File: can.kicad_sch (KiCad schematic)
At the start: 22 parts, among them SW7 CVS-03B, U19 TCAN3414DR, U20 TCAN3414DR

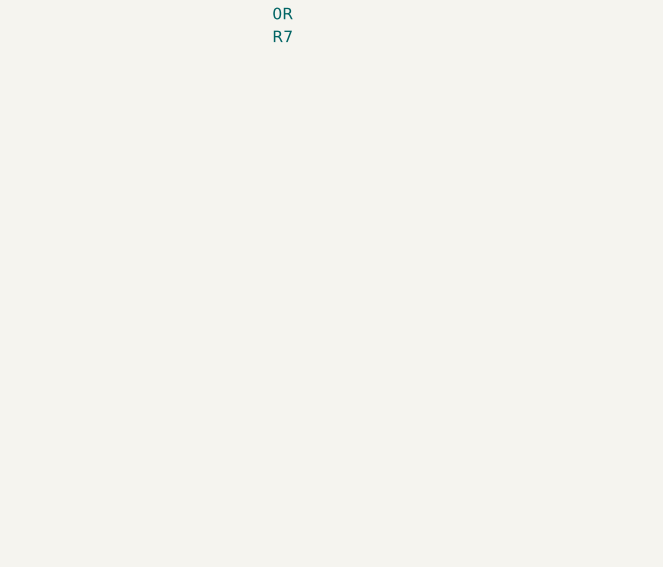
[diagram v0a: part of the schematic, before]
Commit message: [#95398] Implement BGA MCU
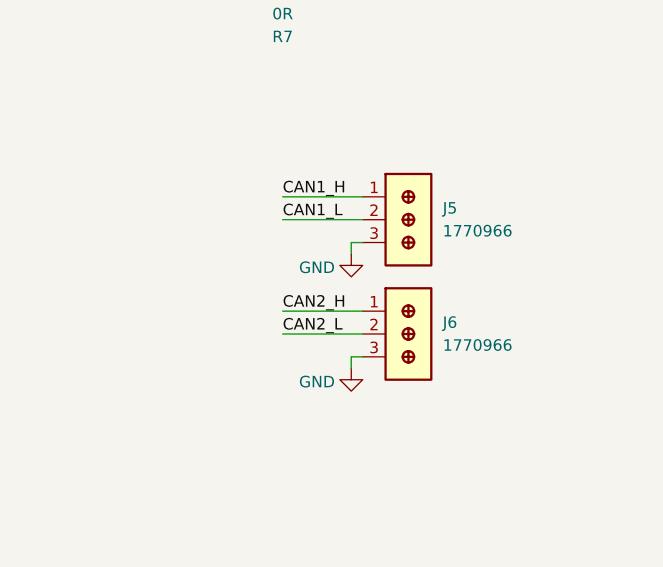
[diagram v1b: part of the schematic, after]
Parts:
- added J5, J6: Wire2Board_1x3_P2.5mm_1770966, antmicro-footprints:TerminalBlock_Wire2Board_1x3_P2.5mm_1770966, symbol antmicroTerminalBlocksConnectors:Wire2Board_1x3_P2.5mm_1770966
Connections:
- net CAN1_H: now also J5.1
- net CAN1_L: now also J5.2
- net CAN2_H: now also J6.1
- net CAN2_L: now also J6.2
- net GND: now also J5.3, J6.3

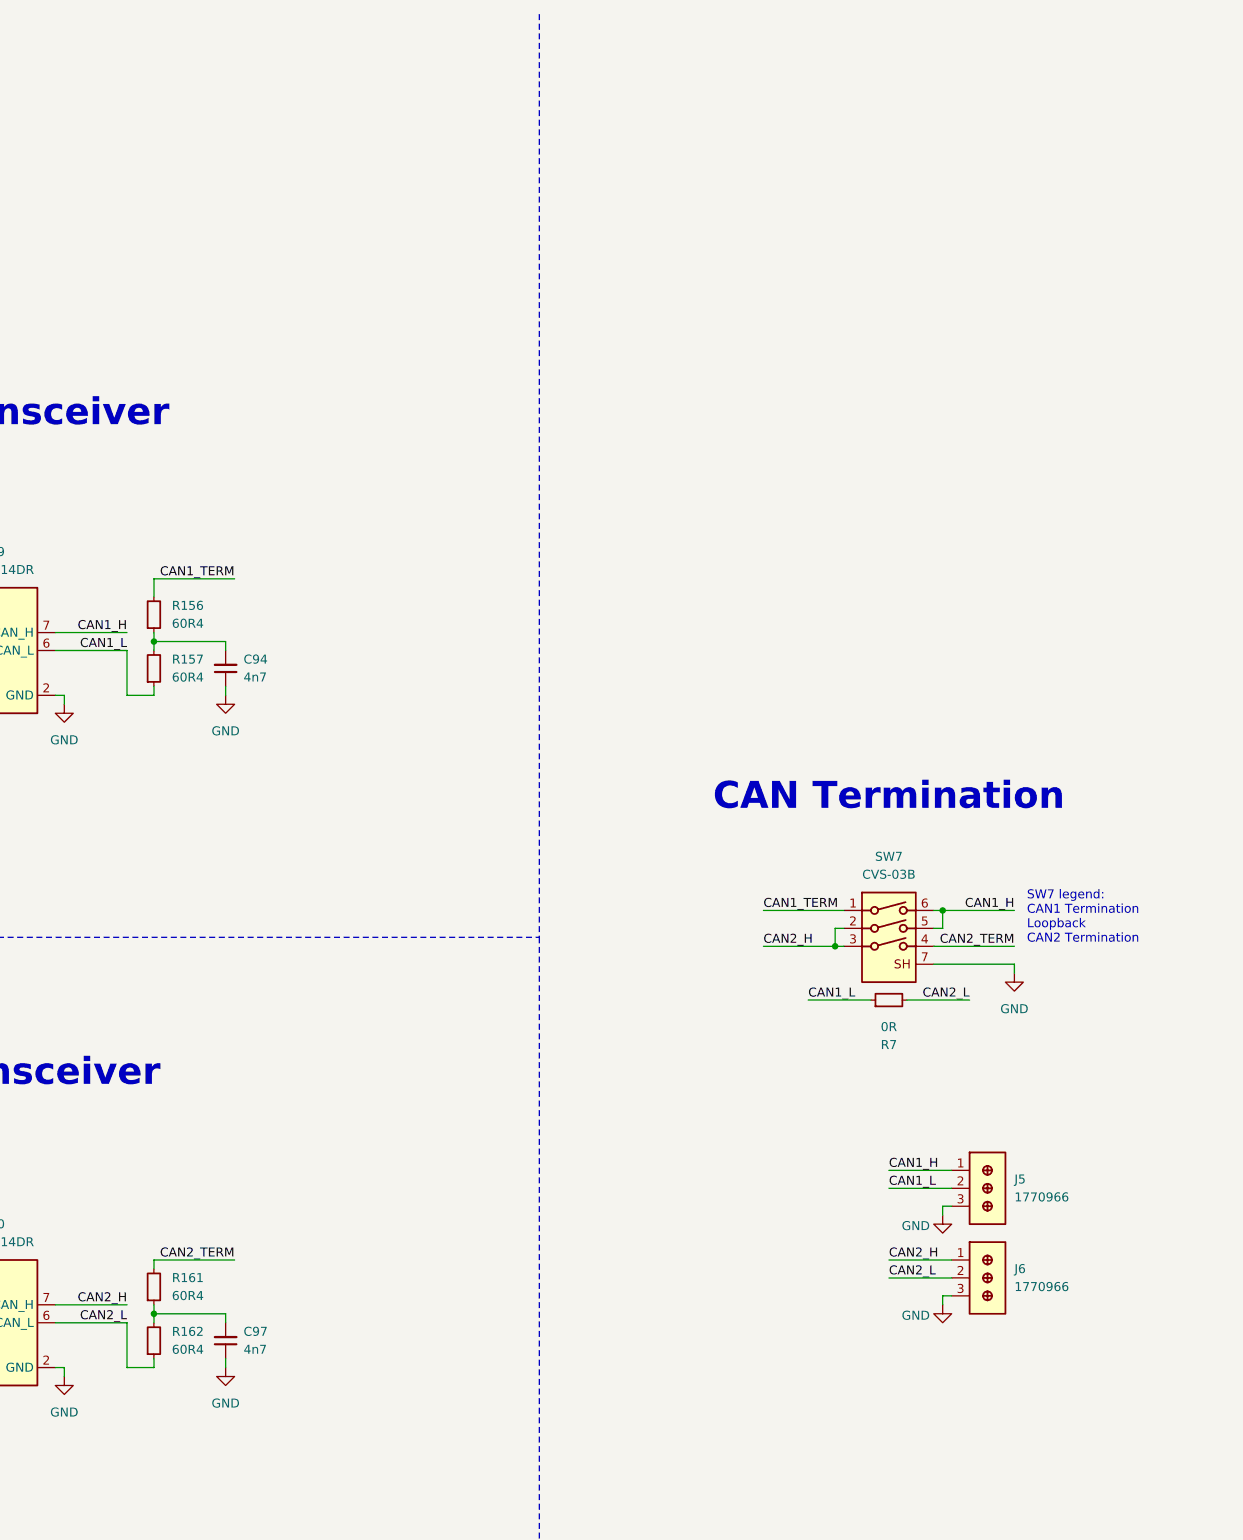
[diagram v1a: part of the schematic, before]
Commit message: [#95398] Edit CAN switching
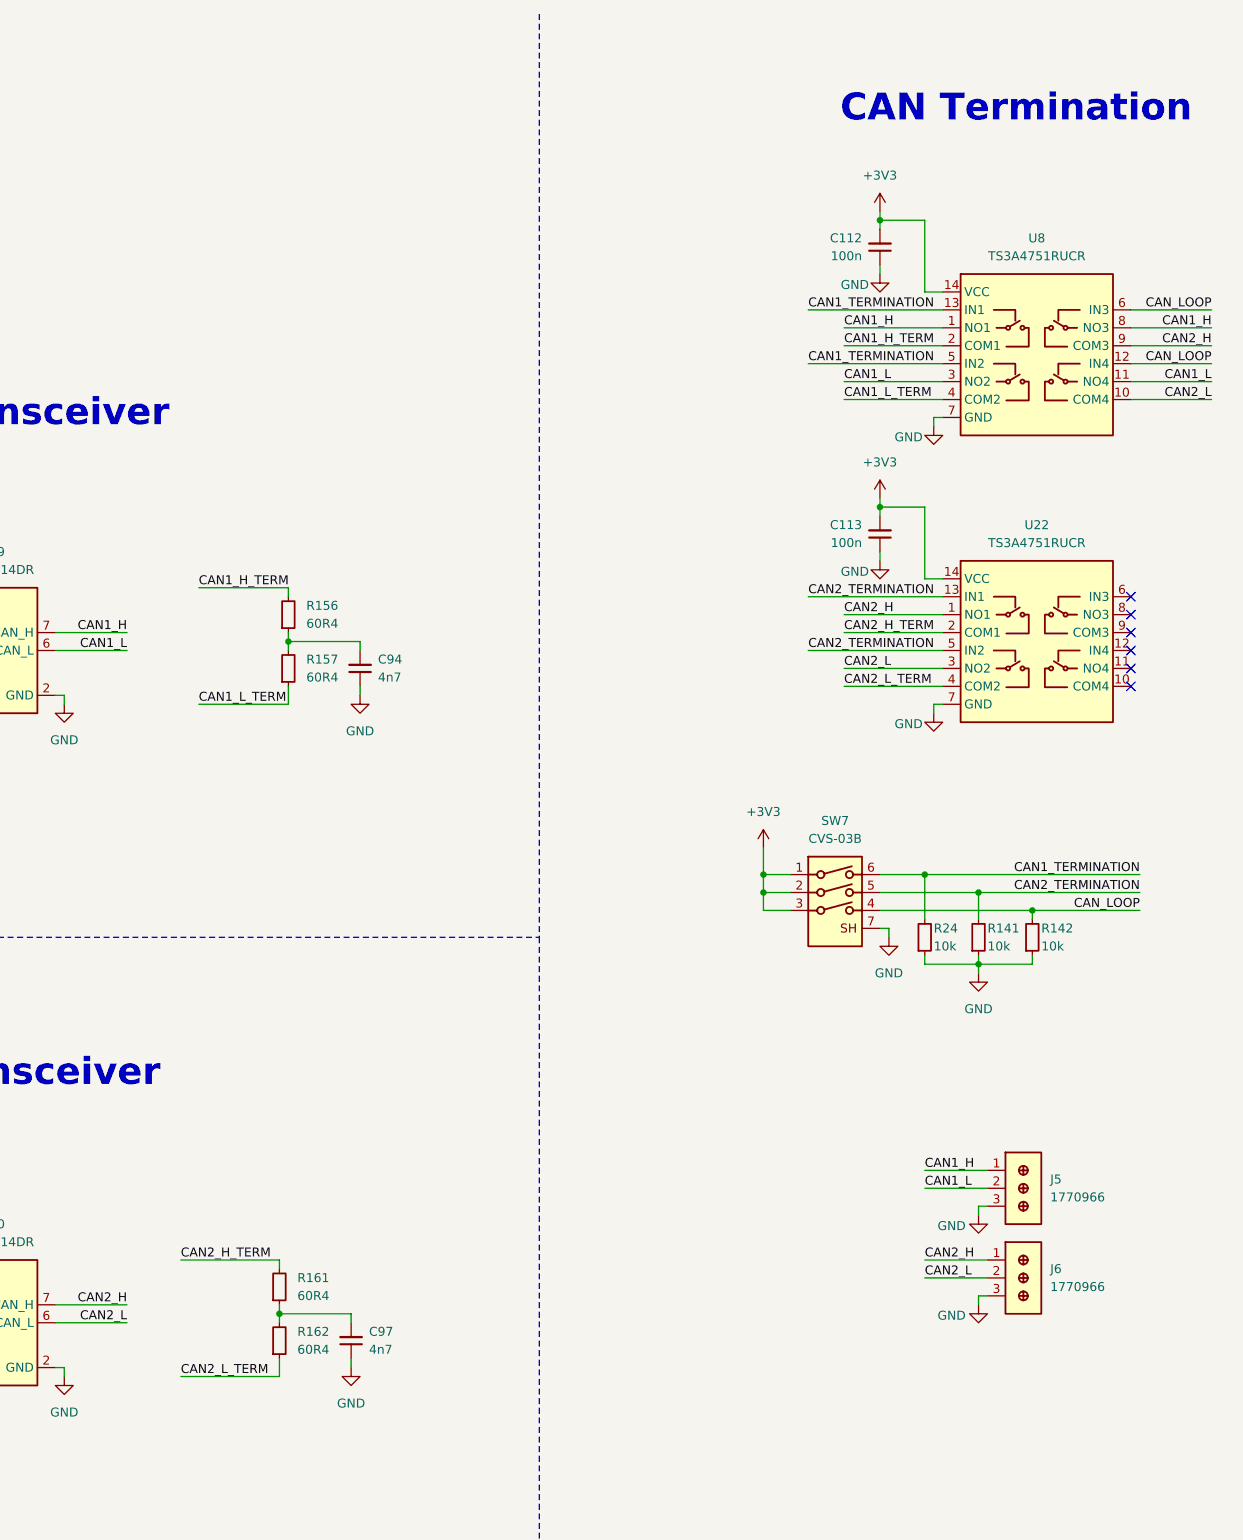
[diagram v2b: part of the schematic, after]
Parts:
- removed R7: R_0R_0402, antmicro-footprints:R_0402_1005Metric, symbol antmicroResistors0402:R_0R_0402
- added C112, C113: C_100n_0402, antmicro-footprints:C_0402_1005Metric, symbol antmicroCapacitors0402:C_100n_0402
- added R141, R142, R24: R_10k_0402, antmicro-footprints:R_0402_1005Metric, symbol antmicroResistors0402:R_10k_0402
- added U22, U8: TS3A4751_X2QFN, antmicro-footprints:Texas_X2QFN-14_2x2mm_P0.4mm, symbol antmicroInterfaceAnalogSwitchesMultiplexersDemultiplexers:TS3A4751_X2QFN
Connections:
- net +3V3: now also SW7.1, SW7.2, SW7.3, C112.2, C113.2, U22.14 (VCC), U8.14 (VCC)
- net CAN1_H: now also U8.1 (NO1), U8.8 (NO3); no longer SW7.5, SW7.6
- net CAN1_L: now also U8.11 (NO4), U8.3 (NO2); no longer R157.1
- net CAN2_H: now also U22.1 (NO1), U8.9 (COM3); no longer SW7.2, SW7.3
- net CAN2_L: now also U22.3 (NO2), U8.10 (COM4); no longer R162.1
- net GND: now also C112.1, C113.1, R141.1, R142.1, R24.1, U22.7 (GND), U8.7 (GND)
- net CAN1_TERM renamed CAN1_H_TERM
- net CAN1_H_TERM: now also U8.2 (COM1); no longer SW7.1
- net CAN2_TERM renamed CAN2_H_TERM
- net CAN2_H_TERM: now also U22.2 (COM1); no longer SW7.4
- new net CAN1_L_TERM: R157.1, U8.4 (COM2)
- new net CAN1_TERMINATION: R24.2, SW7.6, U8.13 (IN1), U8.5 (IN2)
- new net CAN2_L_TERM: R162.1, U22.4 (COM2)
- new net CAN2_TERMINATION: R141.2, SW7.5, U22.13 (IN1), U22.5 (IN2)
- new net CAN_LOOP: R142.2, SW7.4, U8.12 (IN4), U8.6 (IN3)
- no-connect marks 0 -> 6
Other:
- note removed: "SW7 legend: CAN1 Termination Loopback CAN2 Termination"
- moved on the sheet: C94, C97, J5, J6, R156, R157, R161, R162, SW7

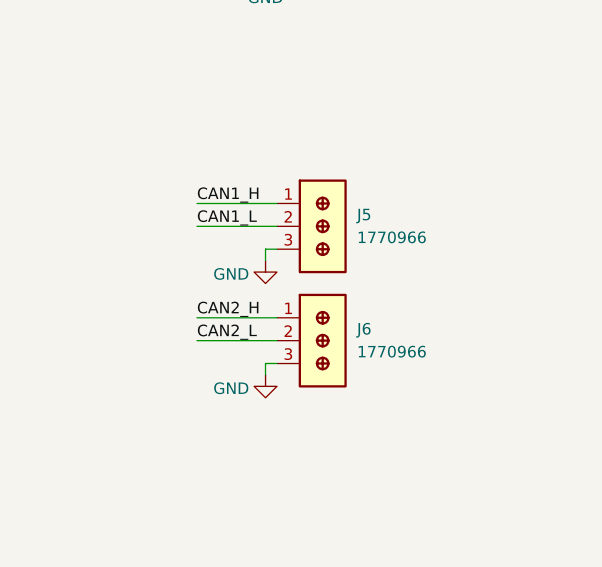
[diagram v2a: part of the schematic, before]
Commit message: [#95398] Replace CAN connectors
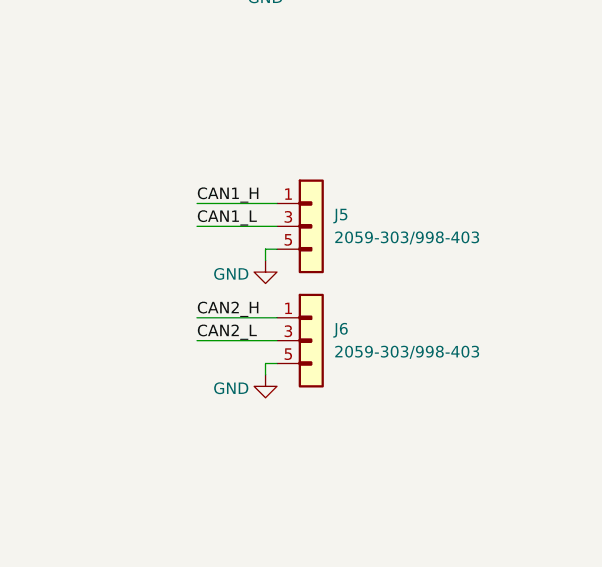
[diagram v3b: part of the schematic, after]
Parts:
- removed J5, J6: Wire2Board_1x3_P2.5mm_1770966, antmicro-footprints:TerminalBlock_Wire2Board_1x3_P2.5mm_1770966, symbol antmicroTerminalBlocksConnectors:Wire2Board_1x3_P2.5mm_1770966
- added J5, J6: Wago_2059_1x3_2059-303/998-403, antmicro-footprints:Wago_2059_1x3_2059-303-998-403, symbol antmicroWire2BoardConnectors:Wago_2059_1x3_2059-303/998-403
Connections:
- net CAN1_H: now also J5.1, J5.2
- net CAN1_L: now also J5.3, J5.4
- net CAN2_H: now also J6.1, J6.2
- net CAN2_L: now also J6.3, J6.4
- net GND: now also J5.5, J5.6, J6.5, J6.6

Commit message: [#95398] Replace WAGO connectors
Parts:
- removed J5, J6: Wago_2059_1x3_2059-303/998-403, antmicro-footprints:Wago_2059_1x3_2059-303-998-403, symbol antmicroWire2BoardConnectors:Wago_2059_1x3_2059-303/998-403
- added J5, J6: Wago_2059_1x3_2059-303/998-403, antmicro-footprints:WAGO_2059_1x3_2059-303-998-403, symbol antmicroWire2BoardConnectors:WAGO_2059_1x3_2059-303/998-403
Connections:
- net CAN1_H: now also J5.1, J5.2
- net CAN1_L: now also J5.3, J5.4
- net CAN2_H: now also J6.1, J6.2
- net CAN2_L: now also J6.3, J6.4
- net GND: now also J5.5, J5.6, J6.5, J6.6

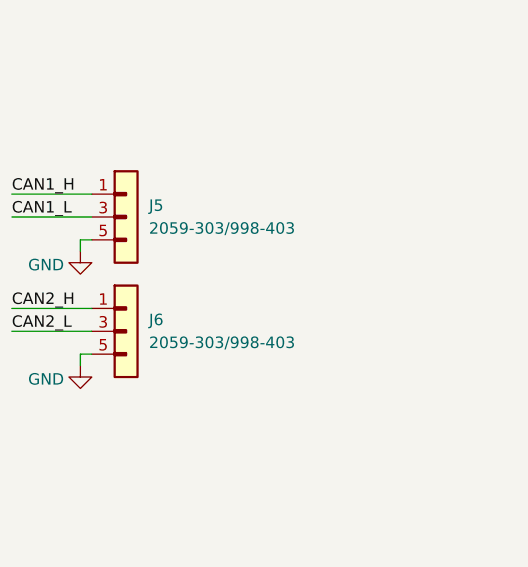
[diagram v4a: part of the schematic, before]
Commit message: [#95398] Update WAGO symbols. Add CAN 3V3 compatibility comment
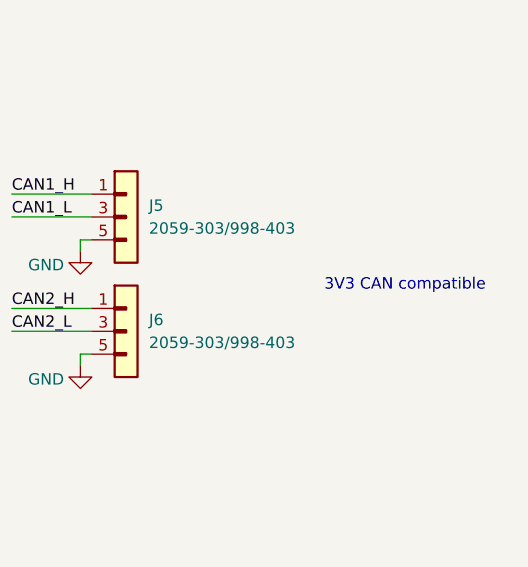
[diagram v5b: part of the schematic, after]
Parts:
- J5, J6: symbol antmicroWire2BoardConnectors:WAGO_2059_1x3_2059-303/998-403 -> Wire2BoardConnectors:WAGO_2059_1x3_2059-303-998-403
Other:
- note added: "3V3 CAN compatible"
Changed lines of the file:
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@@
 		(company "Antmicro")
 	)
+	(text "3V3 CAN compatible"
+		(exclude_from_sim no)
+		(at 333.248 186.69 0)
+		(effects
+			(font
+				(size 1.27 1.27)
+			)
+		)
+	)
 	(text "CAN2 Transceiver"
 		(exclude_from_sim no)
@@
 	)
 	(symbol
-		(lib_id "antmicroWire2BoardConnectors:WAGO_2059_1x3_2059-303/998-403")
+		(lib_id "Wire2BoardConnectors:WAGO_2059_1x3_2059-303-998-403")
 		(at 298.45 189.23 0)
 		(unit 1)
@@
 	)
 	(symbol
-		(lib_id "antmicroWire2BoardConnectors:WAGO_2059_1x3_2059-303/998-403")
+		(lib_id "Wire2BoardConnectors:WAGO_2059_1x3_2059-303-998-403")
 		(at 298.45 176.53 0)
 		(unit 1)

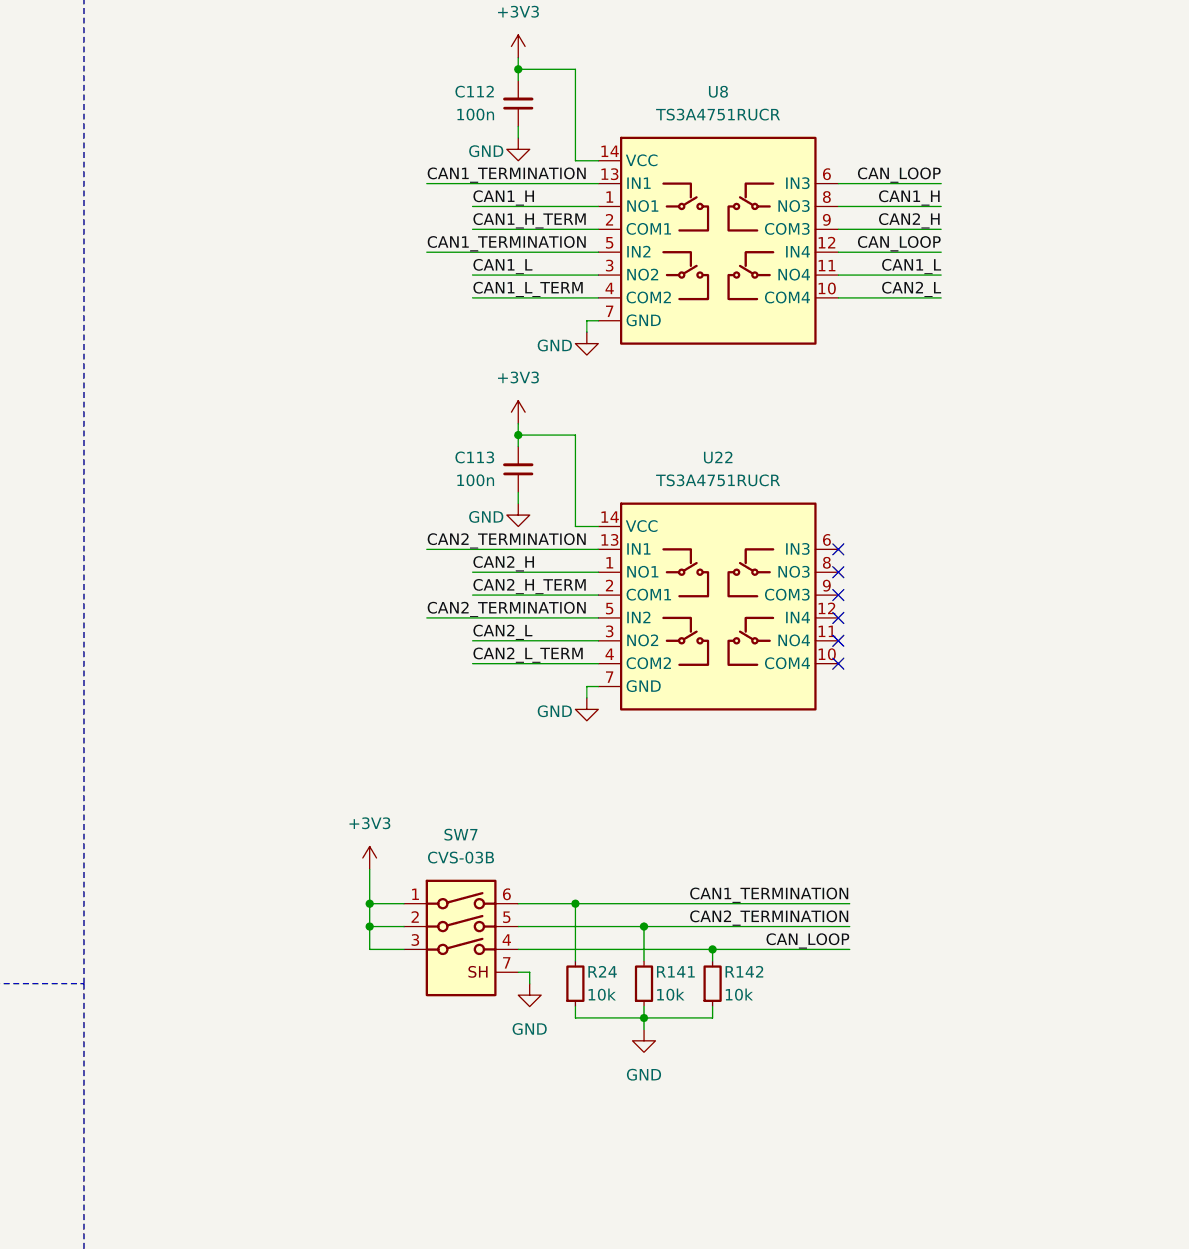
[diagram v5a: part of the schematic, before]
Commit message: [#95451] Improve placement. Add JTAG TC and ID EEPROM.
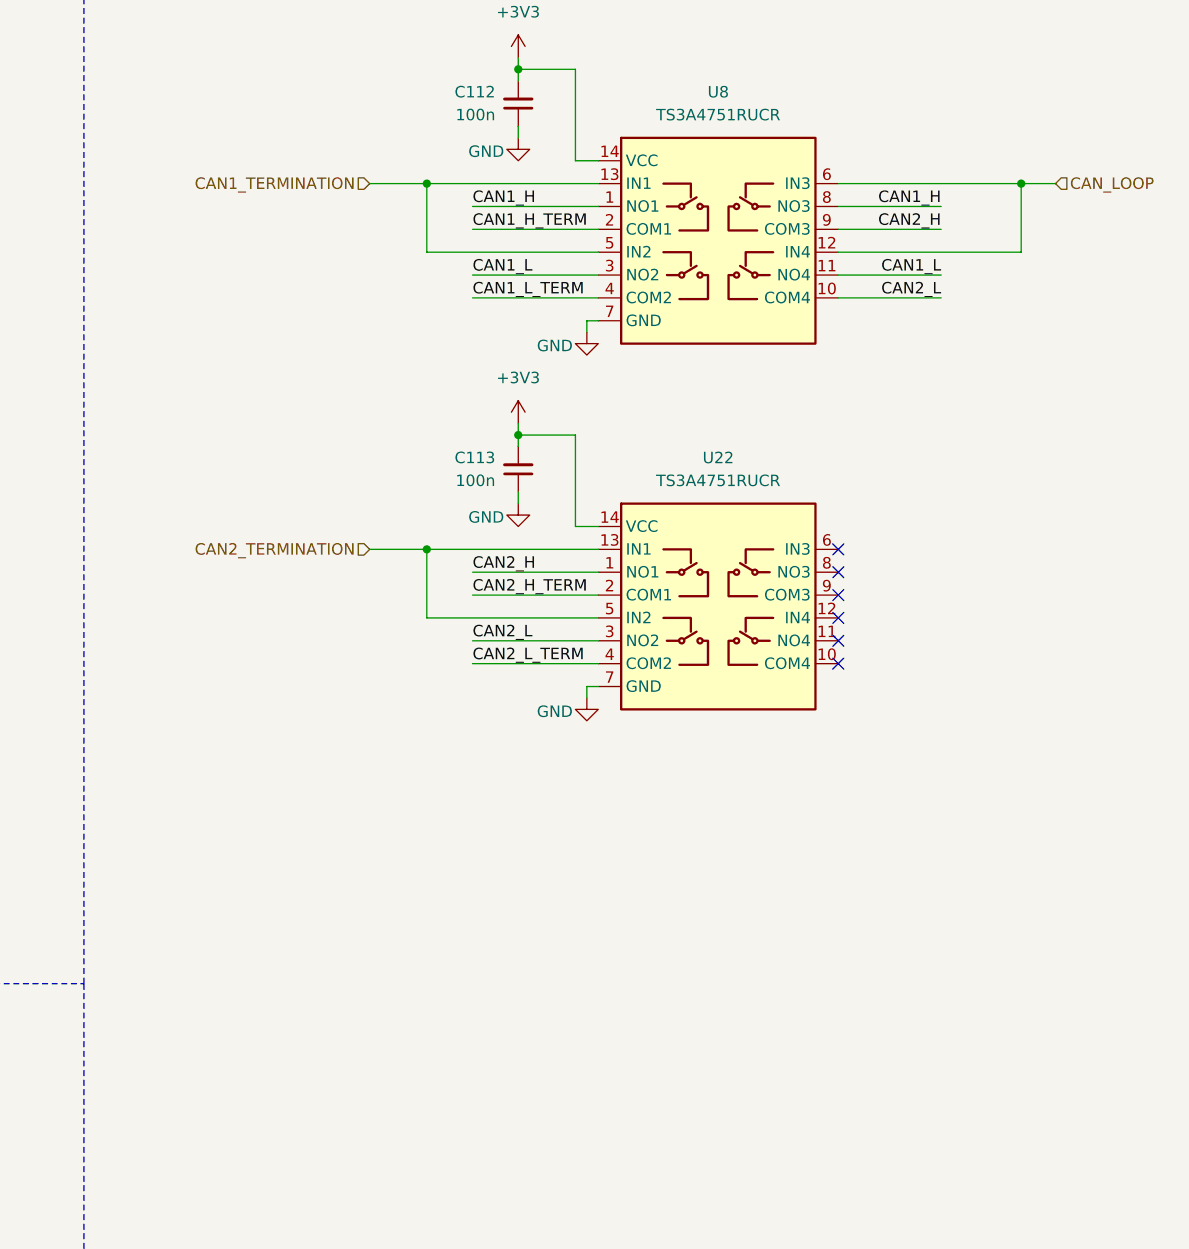
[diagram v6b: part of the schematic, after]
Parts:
- removed R141, R142, R24: R_10k_0402, antmicro-footprints:R_0402_1005Metric, symbol antmicroResistors0402:R_10k_0402
- removed SW7: CVS-03B, antmicro-footprints:SW_DIP_SPSTx03_Slide_Copal_CVS-03xB_W5.9mm_P1mm, symbol antmicroSlideSwitches:CVS-03B
